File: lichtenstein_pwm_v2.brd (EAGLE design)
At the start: 72.1 x 117 mm, 60 parts, among them IC2 MCP23017, IC3 74AHCT125SOIC14, IC5 LM75B, J1 MAGJACK, U1 ONION-OMEGA2

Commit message: power for pwm board
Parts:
- removed C1, C7: 100nF, rcl:C0805
- removed C3: 47µF, rcl:CT7343
- removed C6: 100µF, rcl:CT7343
- added C16: 100µF, rcl:CT7343
- added C17: 47µF, rcl:CT7343
- added C18, C19: 100nF, rcl:C0805
- added R24, R25: 330R, rcl:M0805
- added SV5: 1792889, lichtenstein_onion:1792889
- added U$1: LD1117, lichtenstein_onion:TO220V
- SV1: device con-lstb:MA06-1 -> con-lstb:MA03-1
- moved IC5 198.7 mm to (-51.8, 64.0)
- moved IC4 194.9 mm to (-25.1, 65.8)
- moved C13 178.0 mm to (-50.0, 37.1)
- moved C14 178.0 mm to (-43.7, 37.1)
- moved C15 178.0 mm to (-37.3, 37.1)
- moved C4 178.0 mm to (-61.7, 30.7)
- moved SV2 178.0 mm to (-60.5, 39.6)
- moved C10 167.7 mm to (-37.8, 88.1)
- moved C11 167.7 mm to (-31.5, 88.1)
- moved C12 167.7 mm to (-25.1, 88.1)
- moved C2 167.7 mm to (-56.9, 88.1)
- moved C5 167.7 mm to (-60.2, 95.8)
- moved C8 167.7 mm to (-44.2, 88.1)
- moved C9 167.7 mm to (-40.4, 96.3)
- moved IC2 167.7 mm to (-27.7, 107.2)
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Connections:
- new net N$7: R24.2, SV4.3
- new net N$8: R25.2, SV5.3
- net +3V3: now also C16.+, C19.1, U$1.2; no longer C6.+, C7.1, SV1.3
- net CONSOLE_RX: now also SV1.3; no longer SV1.5
- net CONSOLE_TX: now also SV1.2; no longer SV1.4
- net GND: now also C16.-, C17.-, C18.2, C19.2, SV5.2, SV5.4, U$1.1; no longer C1.2, C3.-, C6.-, C7.2
- net PWMOUT0: now also R24.1; no longer SV4.1
- net PWMOUT1: now also R25.1; no longer SV4.3
- net V+: now also C17.+, C18.1, SV4.1, SV5.1, U$1.3; no longer C1.1, C3.+
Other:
- board size 72.1 x 117 mm -> 71.9 x 117 mm
- board text added: "Lichtenstein Omega2 PWM © 2018 Tristan Seifert"
- board text removed: "Lichtenstein Differential Output © 2018 Tristan Seifert"

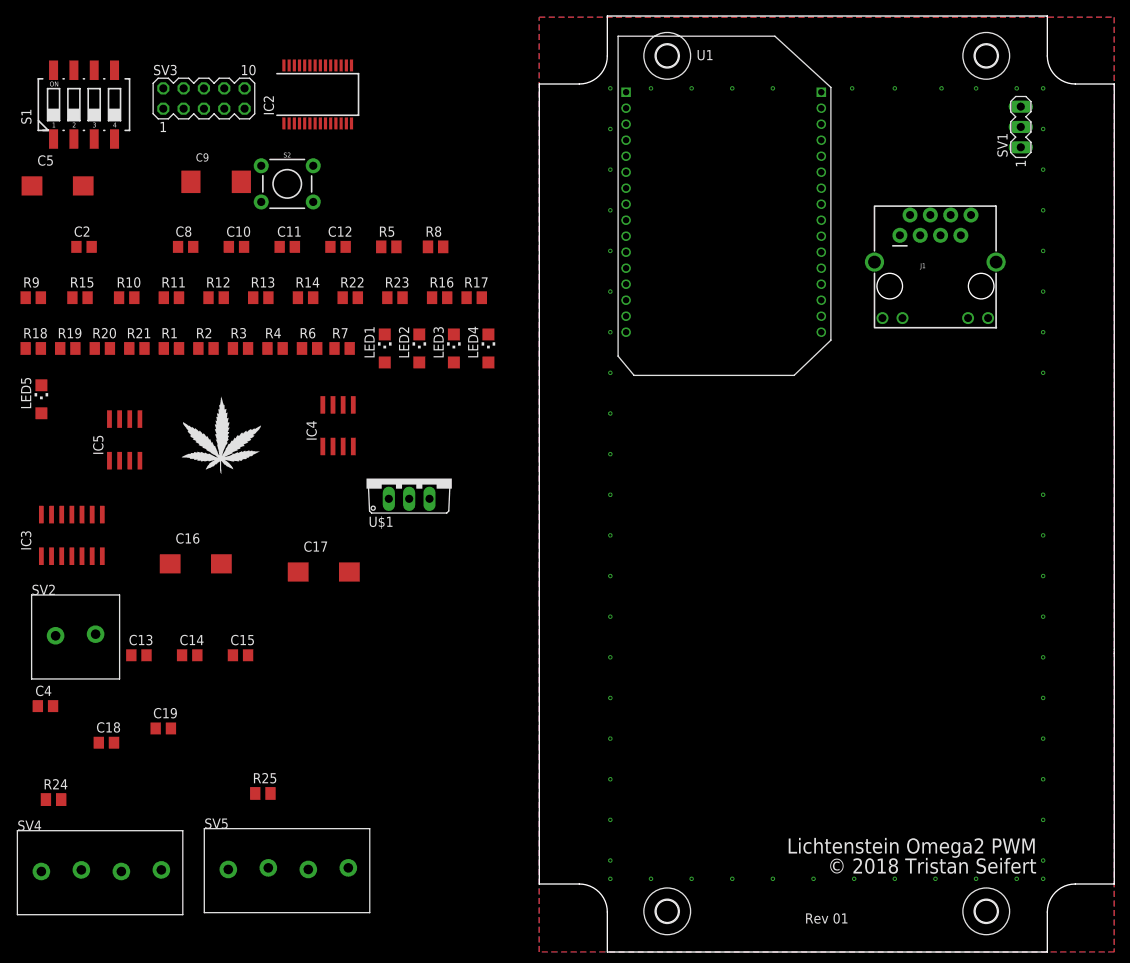
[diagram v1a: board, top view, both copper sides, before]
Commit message: routed most of the pwm board, need to finish with input connectors
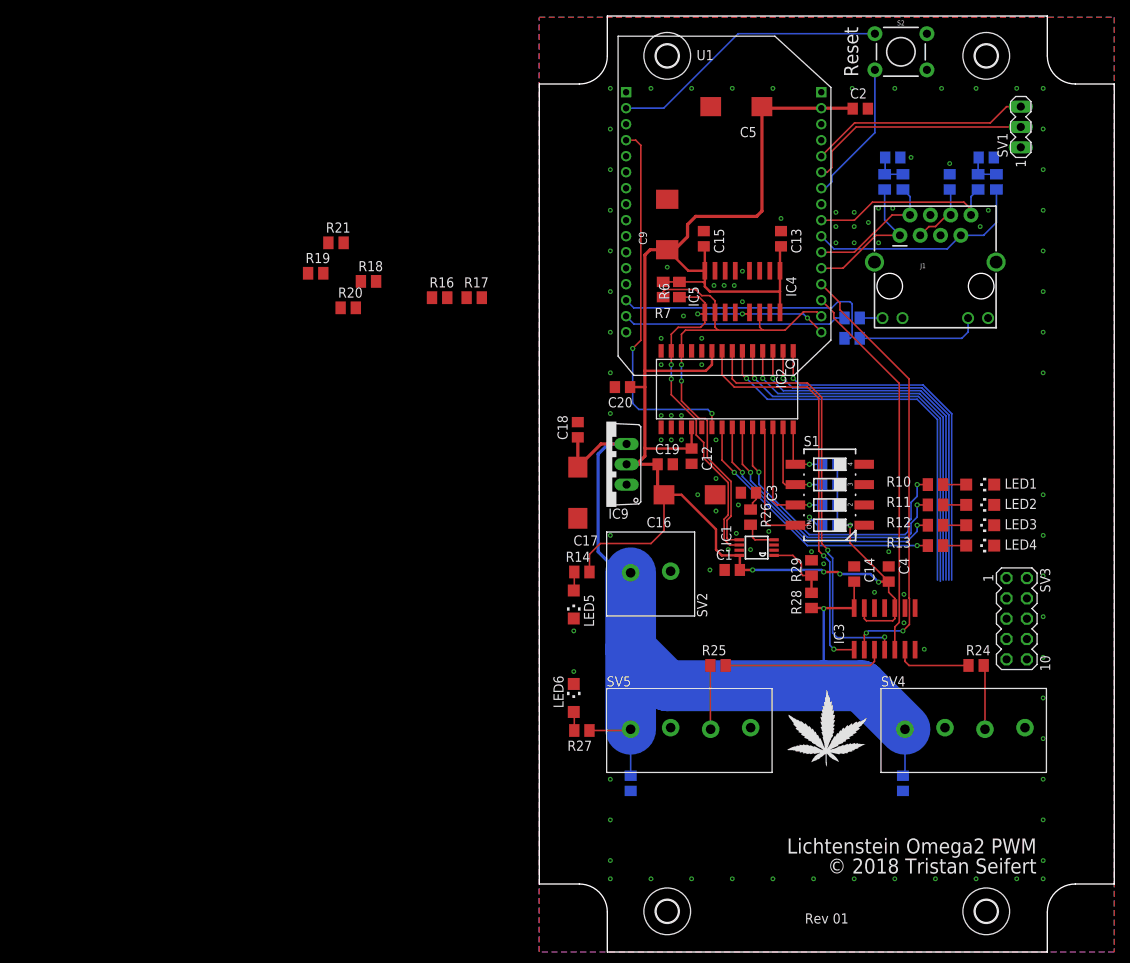
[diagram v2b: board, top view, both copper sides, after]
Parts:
- removed U$1: LD1117, lichtenstein_onion:TO220V
- added C1, C20, C3, C6, C7: 100nF, rcl:C0805
- added IC1: MAX11647, lichtenstein_onion:UMAX8
- added IC9: LD1117, lichtenstein_onion:TO220V
- added LED6: (no value), led:CHIPLED_1206
- added R26: 2k, rcl:M0805
- added R27: 1k2, rcl:M0805
- added R28: 3k09, rcl:M0805
- added R29: 1k07, rcl:M0805
- IC2: device lichtenstein_onion:SSOP28 -> lichtenstein_onion:SO28W
- R11, R12, R13, R14: value 680R -> 470R
- moved SV3 120.6 mm to (59.7, 41.7), turned to 270 degrees
- moved R24 116.5 mm to (54.6, 35.8)
- moved SV4 109.4 mm to (53.3, 27.9)
- moved R9 107.4 mm to (43.2, 96.3), flipped to the bottom, turned to 90 degrees
- moved C4 106.7 mm to (43.7, 47.2), turned to 270 degrees
- moved S1 105.2 mm to (36.3, 57.1), turned to 90 degrees
- moved R15 103.9 mm to (45.5, 96.3), flipped to the bottom, turned to 90 degrees
- moved R10 103.8 mm to (49.5, 58.4)
- moved IC3 102.3 mm to (43.2, 40.4)
- moved C8 100.7 mm to (55.9, 99.3), flipped to the bottom
- moved R11 99.0 mm to (49.5, 55.9)
- moved C2 98.6 mm to (40.1, 105.4)
- moved C13 95.7 mm to (30.2, 89.2), turned to 270 degrees
- moved R12 94.3 mm to (49.5, 53.3)
- moved R13 89.8 mm to (49.5, 50.8)
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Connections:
- new net CURRENT: IC1.2
- new net N$12: IC1.4, R26.1
- new net N$13: C3.2, R26.2
- new net N$14: LED6.A, R27.2
- new net VIN_DIVIDED: IC1.1, R28.1, R29.2
- net +3V3: now also C1.2, C20.1, IC1.8, IC9.2; no longer U$1.2
- net GND: now also C1.1, C20.2, C3.1, C6.2, C7.2, IC1.7, IC4.7, IC9.1, LED6.C, R29.1; no longer U$1.1
- net I2C_SCL: now also IC1.5
- net I2C_SDA: now also IC1.6
- net TEST0: now also S1.8; no longer S1.5
- net TEST1: now also S1.7; no longer S1.6
- net TEST2: now also S1.6; no longer S1.7
- net TEST3: now also S1.5; no longer S1.8
- net V+: now also C6.1, C7.1, IC9.3, R27.1, R28.2; no longer U$1.3
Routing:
- net +3V3: track 0.00 -> 214.0 mm, vias 0 -> 5
- net V+: track 0.00 -> 125.8 mm, vias 0 -> 1
- net I2C_SCL: track 0.00 -> 63.3 mm, vias 0 -> 2
- net I2C_SDA: track 0.00 -> 60.1 mm, vias 0 -> 5
- net PWM0: track 0.00 -> 55.1 mm, vias 0 -> 2
- net !PWM1_OE: track 0.00 -> 54.0 mm, vias 0 -> 2
- net !PWM0_OE: track 0.00 -> 51.0 mm, vias 0 -> 2
- net INPUT2: track 0.00 -> 49.8 mm, vias 0 -> 1
- net INPUT3: track 0.00 -> 49.2 mm, vias 0 -> 1
- net INPUT1: track 0.00 -> 48.4 mm, vias 0 -> 1
- net PWM1: track 0.00 -> 48.0 mm
- net INPUT5: track 0.00 -> 47.7 mm, vias 0 -> 1
- net I2C_INT: track 0.00 -> 46.9 mm, vias 0 -> 2
- net INPUT0: track 0.00 -> 46.7 mm, vias 0 -> 1
- net INPUT4: track 0.00 -> 45.9 mm, vias 0 -> 1
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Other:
- outline, holes or cut-outs redrawn
- board text added: "Reset"

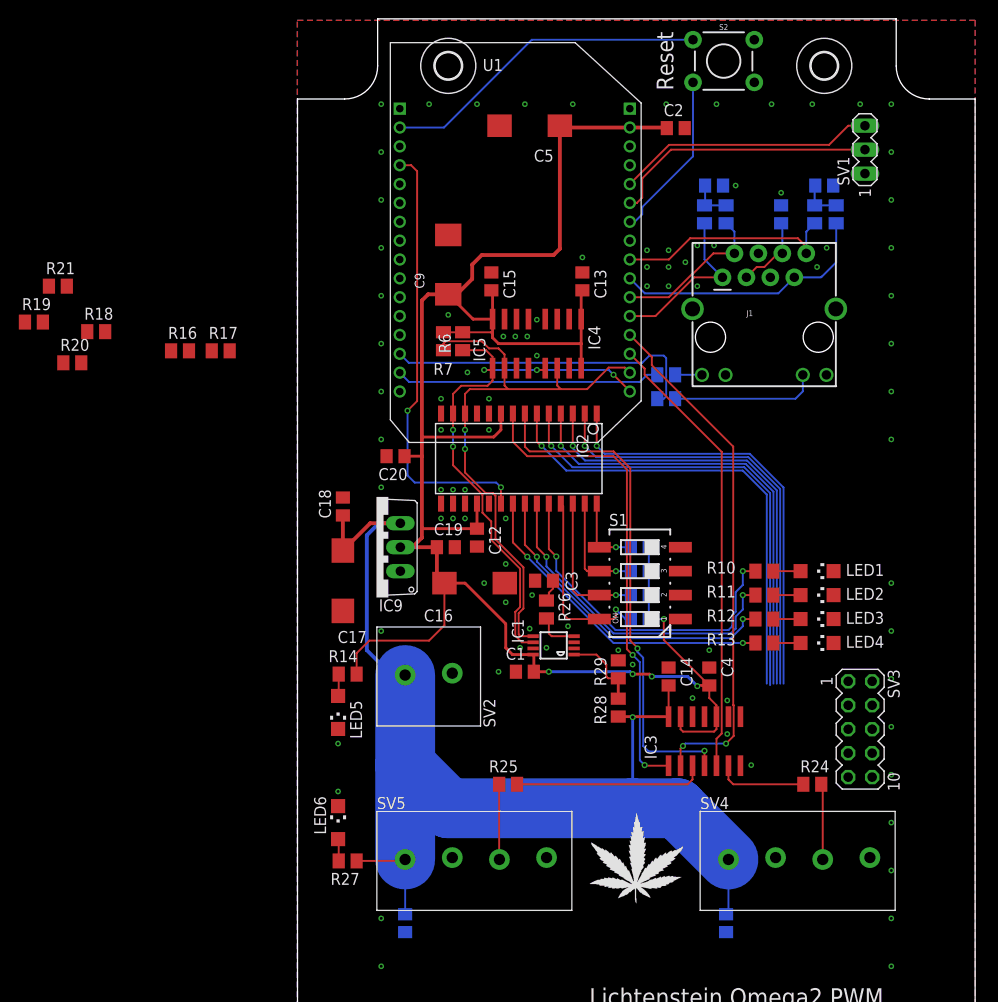
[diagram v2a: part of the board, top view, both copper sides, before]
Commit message: finished routing PWMv2 board
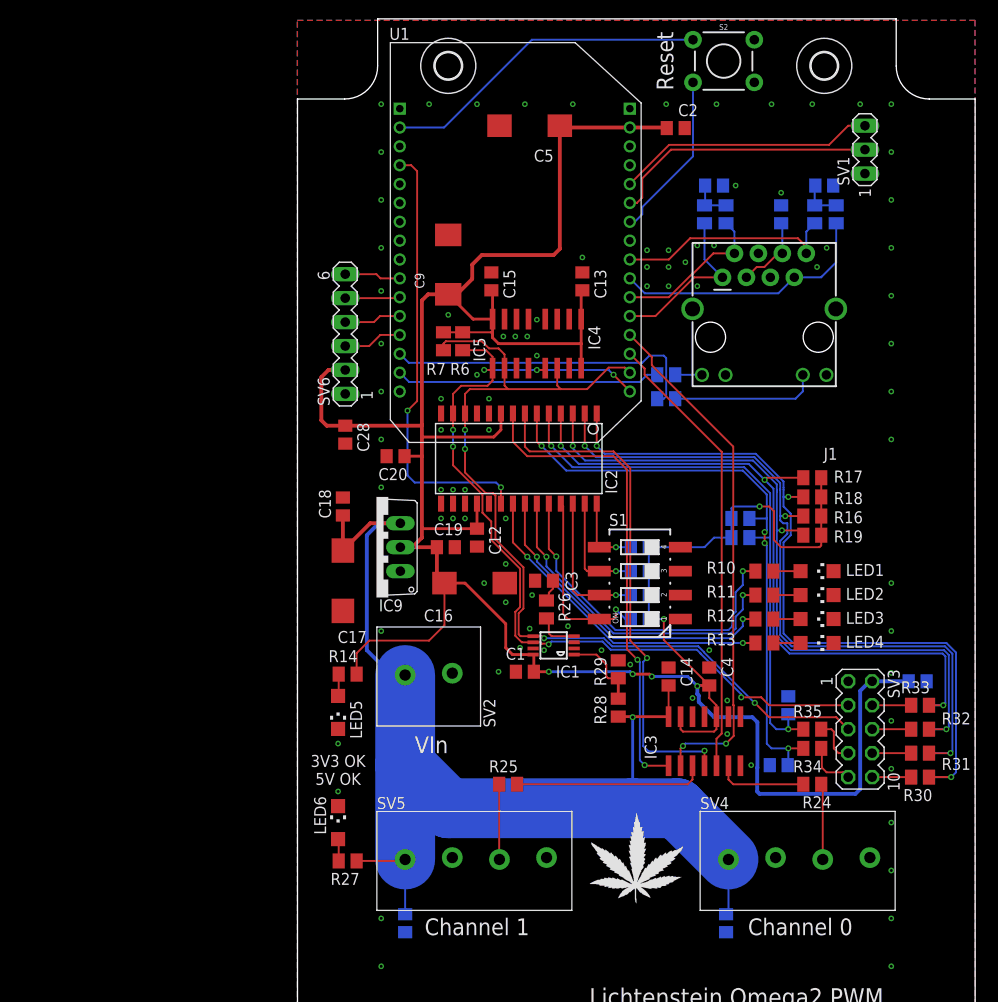
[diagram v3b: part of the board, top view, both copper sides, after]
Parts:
- added C21, C22, C23, C24, C25, C26, C27, C28: 100nF, rcl:C0805
- added R30, R31, R32, R33, R34, R35: 10k, rcl:M0805
- added SV6: (no value), con-lstb:MA06-1
- moved R19 85.6 mm to (54.6, 62.2)
- moved R18 77.9 mm to (54.6, 66.3)
- moved R21 77.1 mm to (47.0, 62.0), flipped to the bottom
- moved R20 72.8 mm to (47.0, 64.0), flipped to the bottom
- moved R16 69.3 mm to (54.6, 64.3)
- moved R17 64.2 mm to (54.6, 68.3)
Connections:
- new net N$15: R30.1, SV3.10
- new net N$16: R31.1, SV3.8
- new net N$17: R32.1, SV3.6
- new net N$18: R33.1, SV3.4
- new net N$19: R34.1, SV3.9
- new net N$20: R35.1, SV3.7
- net !SPI_CS: now also SV6.3
- net +3V3: now also C27.2, C28.1, SV3.2, SV6.2
- net GND: now also C21.1, C22.1, C23.1, C24.1, C25.1, C26.1, C27.1, C28.2, SV6.1
- net I2C_SCL: now also SV3.5
- net I2C_SDA: now also SV3.3
- net INPUT0: now also C21.2, R31.2; no longer SV3.4
- net INPUT1: now also C22.2, R33.2; no longer SV3.6
- net INPUT2: now also C23.2, R34.2; no longer SV3.8
- net INPUT3: now also C24.2, R35.2; no longer SV3.10
- net INPUT4: now also C25.2, R30.2; no longer SV3.3
- net INPUT5: now also C26.2, R32.2; no longer SV3.5
- net SPI_MISO: now also SV6.6
- net SPI_MOSI: now also SV6.5
- net SPI_SCK: now also SV6.4
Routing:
- net +3V3: track 214.0 -> 308.5 mm, vias 5 -> 6
- net I2C_SCL: track 63.3 -> 100.8 mm, vias 2 -> 4
- net I2C_SDA: track 60.1 -> 96.7 mm, vias 5 -> 7
- net INPUT4: track 45.9 -> 80.9 mm, vias 1 -> 3
- net INPUT0: track 46.7 -> 79.5 mm, vias 1 -> 3
- net INPUT5: track 47.7 -> 76.8 mm, vias 1 -> 3
- net INPUT1: track 48.4 -> 75.2 mm, vias 1 -> 3
- net INPUT2: track 49.8 -> 64.0 mm, vias 1 -> 4
- net INPUT3: track 49.2 -> 60.8 mm, vias 1 -> 2
- net !SPI_CS: track 0.00 -> 6.27 mm
- net SPI_SCK: track 0.00 -> 6.04 mm
- net SPI_MISO: track 0.00 -> 5.96 mm
- net SPI_MOSI: track 0.00 -> 5.82 mm
- net N$19: track 0.00 -> 5.27 mm
- net N$20: track 0.00 -> 4.95 mm
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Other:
- board text added: "3V3 OK 5V OK"
- board text added: "Channel 0"
- board text added: "Channel 1"
- board text added: "VIn"

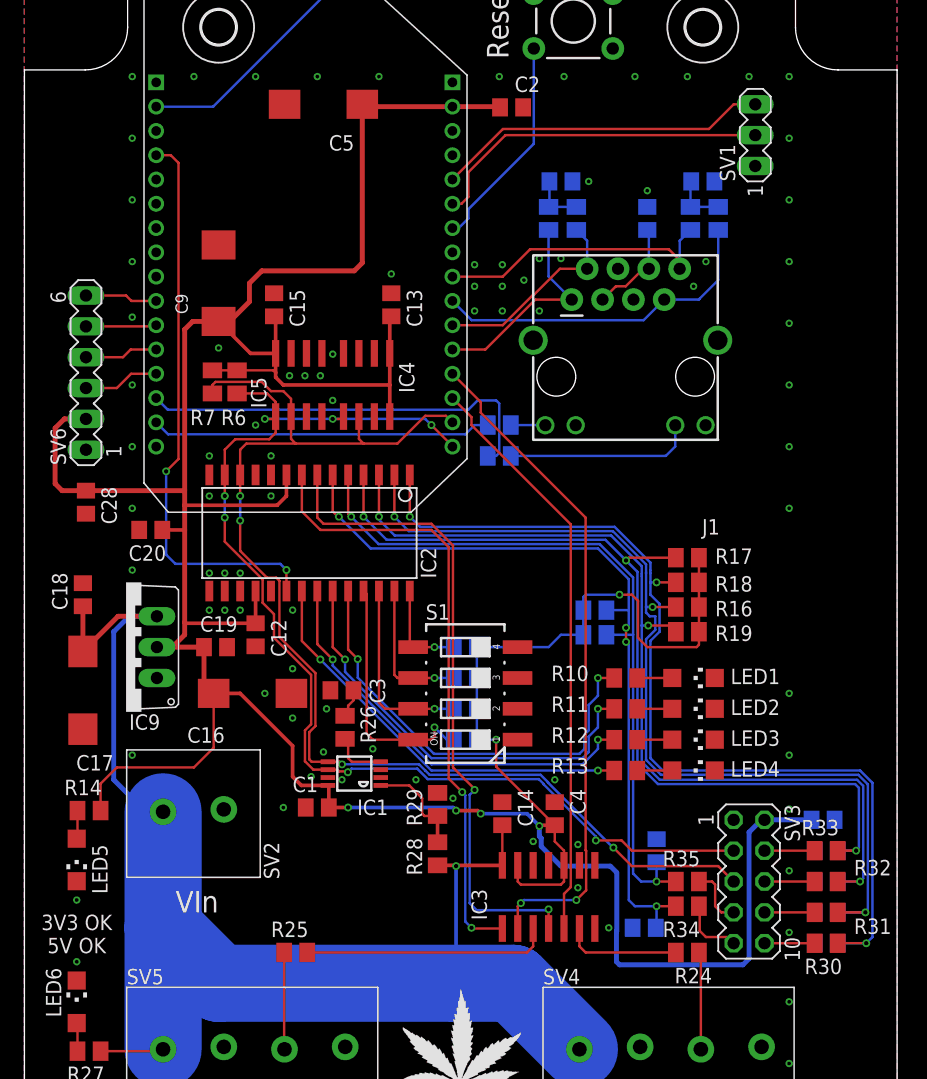
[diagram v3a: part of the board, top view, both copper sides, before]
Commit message: added current sense amplifier; replaced footprints of some large resevoir caps
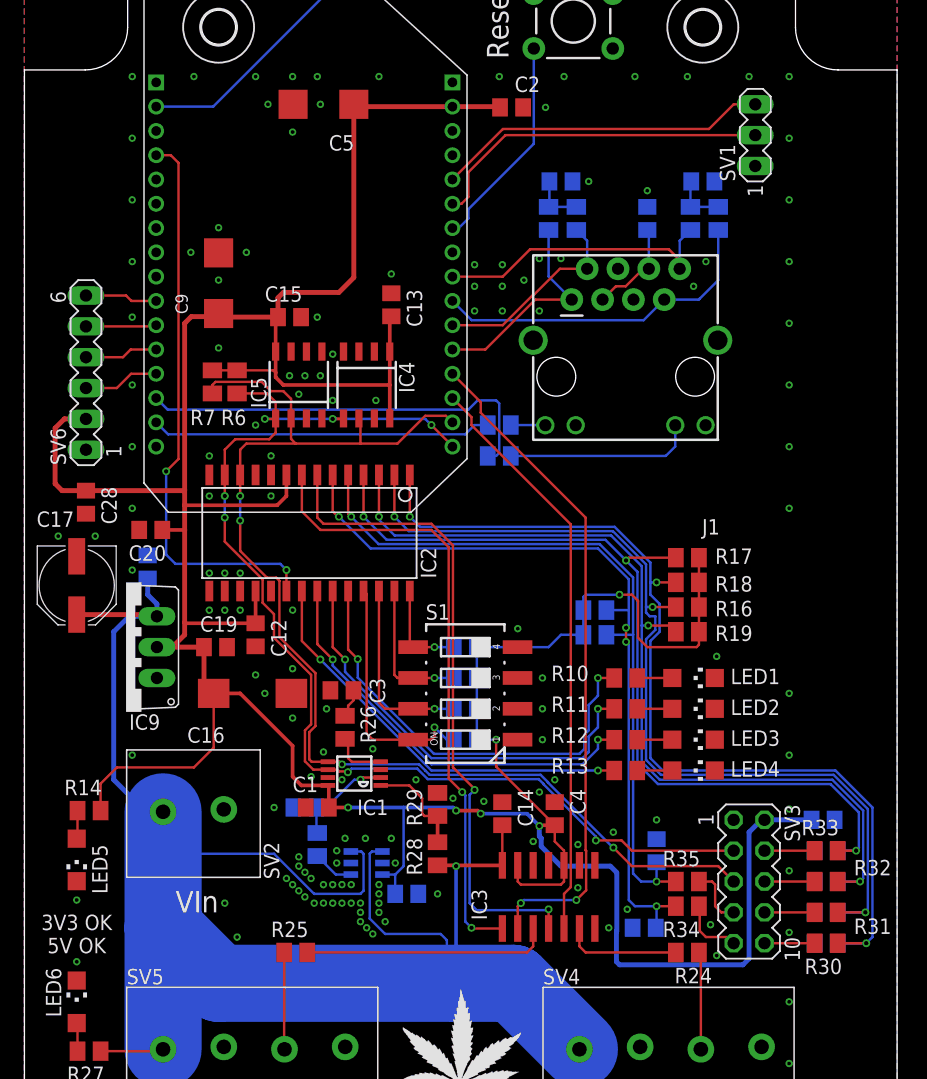
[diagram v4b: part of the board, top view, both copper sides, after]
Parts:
- added C29, C30: 100nF, rcl:C0805
- added IC6: (no value), lichtenstein_onion:SOT23-6L
- added R36: 330R, rcl:M0805
- C17: value 47µF -> 100µF; device rcl:CT7343 -> rcl:PANASONIC_D
- C5: device rcl:CT7343 -> rcl:SMC_C
- C9: device rcl:SMC_D -> rcl:SMC_C
- moved C17 8.65 mm to (4.32, 66.0)
- moved C18 5.80 mm to (10.2, 67.6), flipped to the bottom
- moved C15 1.63 mm to (21.8, 88.1), turned to 180 degrees
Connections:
- new net N$21: IC6.1, R36.2
- new net SENSE+: IC6.3
- new net SENSE-: IC6.4
- net +3V3: now also C29.2, IC6.6
- net CURRENT: now also C30.1, R36.1
- net GND: now also C29.1, C30.2, IC6.2, IC6.5
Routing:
- net SENSE+: track 0.00 -> 19.6 mm
- net SENSE-: track 0.00 -> 18.9 mm
- net CURRENT: track 0.00 -> 8.44 mm, vias 0 -> 1
- net +3V3: track 308.5 -> 313.0 mm
- net N$21: track 0.00 -> 3.40 mm
- net INPUT5: track 76.8 -> 75.6 mm
- net INPUT4: track 80.9 -> 79.7 mm
- net INPUT0: track 79.5 -> 78.3 mm
- net INPUT1: track 75.2 -> 74.0 mm
- net V+: track 125.8 -> 124.8 mm
- net I2C_SDA: track 96.7 -> 97.3 mm
